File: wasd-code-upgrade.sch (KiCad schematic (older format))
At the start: 22 parts, among them J101 Conn_ARM_JTAG_SWD_10, J102 TC2030, Q101 ZXTN08400BFF, Q102 ZXTP25020CFFTA, U101 STM32L422CBTx, U102 MIC5205-3.3YM5

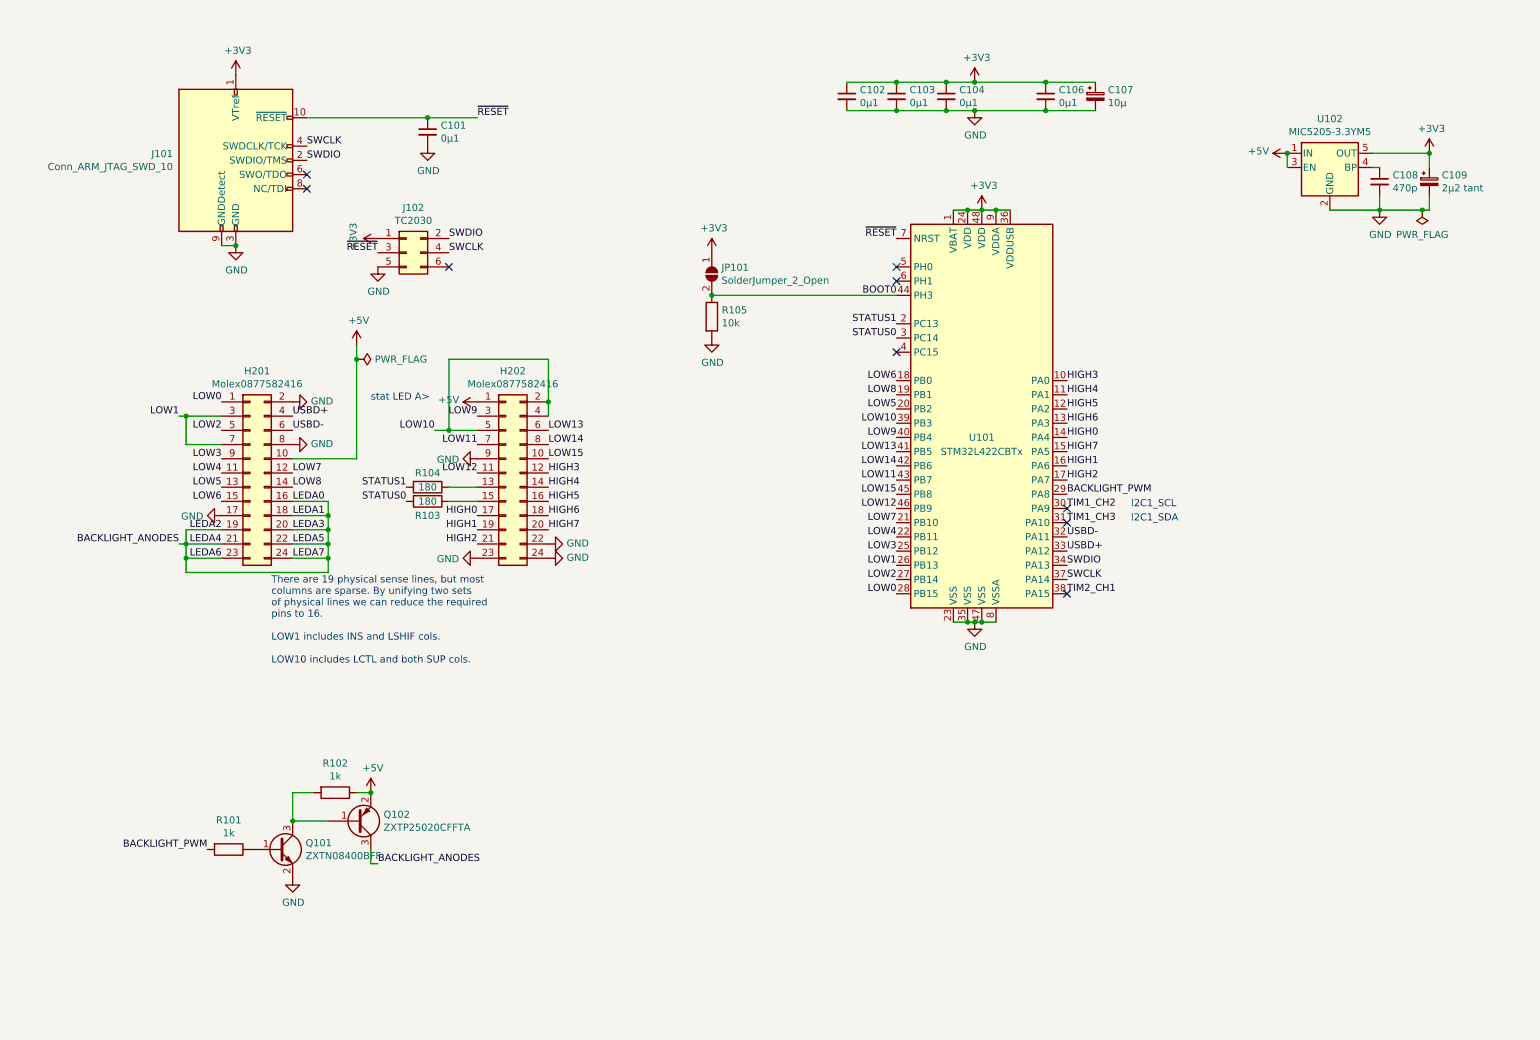
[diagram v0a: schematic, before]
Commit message: wasd-code-upgrade: schematic polish, matrix table
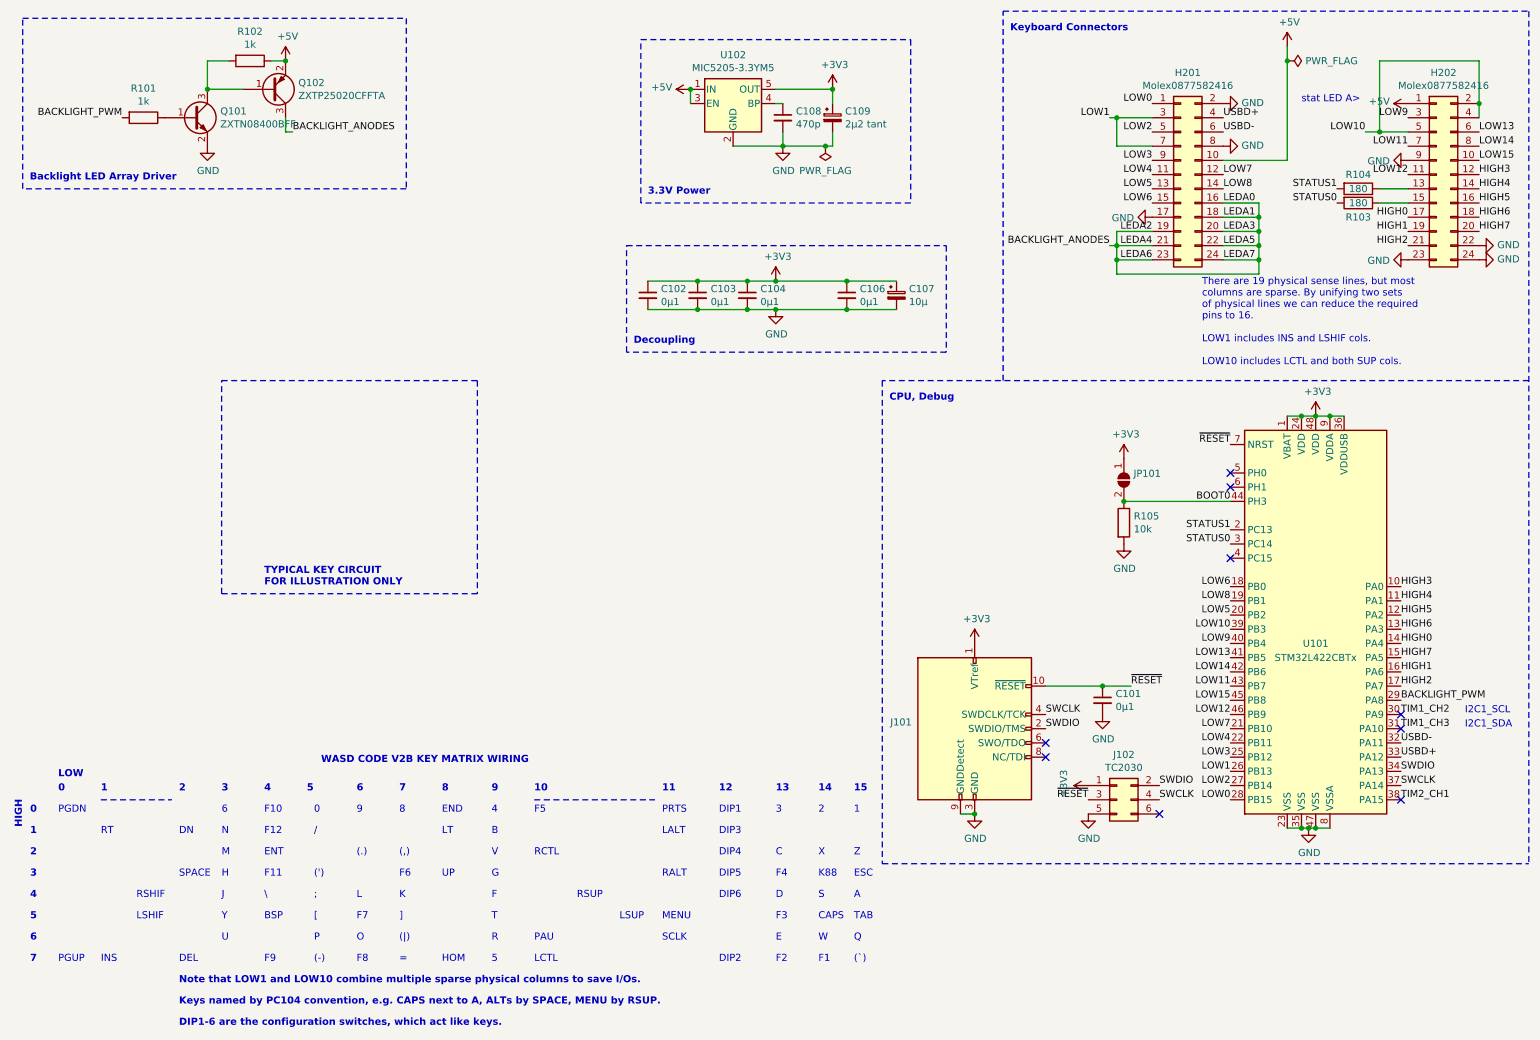
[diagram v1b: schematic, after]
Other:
- note added: "(')"
- note added: "(,)"
- note added: "(-)"
- note added: "(.)"
- note added: "(`)"
- note added: "(|)"
- note added: "/"
- note added: "0"
- note added: "1"
- note added: "10"
- note added: "11"
- note added: "12"
- note added: "13"
- note added: "14"
- note added: "15"
- note added: "2"
- note added: "3"
- note added: "3.3V Power"
- note added: "4"
- note added: "5"
- note added: "6"
- note added: "7"
- note added: "8"
- note added: "9"
- note added: ";"
- note added: "="
- note added: "A"
- note added: "B"
- note added: "BSP"
- note added: "Backlight LED Array Driver"
- note added: "C"
- note added: "CAPS"
- note added: "CPU, Debug"
- note added: "D"
- note added: "DEL"
- note added: "DIP1"
- note added: "DIP1-6 are the configuration switches, which act like keys."
- note added: "DIP2"
- note added: "DIP3"
- note added: "DIP4"
- note added: "DIP5"
- note added: "DIP6"
- note added: "DN"
- note added: "Decoupling"
- note added: "E"
- note added: "END"
- note added: "ENT"
- note added: "ESC"
- note added: "F"
- note added: "F1"
- note added: "F10"
- note added: "F11"
- note added: "F12"
- note added: "F2"
- note added: "F3"
- note added: "F4"
- note added: "F5"
- note added: "F6"
- note added: "F7"
- note added: "F8"
- note added: "F9"
- note added: "G"
- note added: "H"
- note added: "HIGH"
- note added: "HOM"
- note added: "INS"
- note added: "J"
- note added: "K"
- note added: "K88"
- note added: "Keyboard Connectors"
- note added: "Keys named by PC104 convention, e.g. CAPS next to A, ALTs by SPACE, MENU by RSUP."
- note added: "L"
- note added: "LALT"
- note added: "LCTL"
- note added: "LOW"
- note added: "LSHIF"
- note added: "LSUP"
- note added: "LT"
- note added: "M"
- note added: "MENU"
- note added: "N"
- note added: "Note that LOW1 and LOW10 combine multiple sparse physical columns to save I/Os."
- note added: "O"
- note added: "P"
- note added: "PAU"
- note added: "PGDN"
- note added: "PGUP"
- note added: "PRTS"
- note added: "Q"
- note added: "R"
- note added: "RALT"
- note added: "RCTL"
- note added: "RSHIF"
- note added: "RSUP"
- note added: "RT"
- note added: "S"
- note added: "SCLK"
- note added: "SPACE"
- note added: "T"
- note added: "TAB"
- note added: "TYPICAL KEY CIRCUIT\nFOR ILLUSTRATION ONLY"
- note added: "U"
- note added: "UP"
- note added: "V"
- note added: "W"
- note added: "WASD CODE V2B KEY MATRIX WIRING"
- note added: "X"
- note added: "Y"
- note added: "Z"
- note added: "["
- note added: "\"
- note added: "]"
- moved on the sheet: C101, C102, C103, C104, C106, C107, C108, C109, H201, H202, J101, J102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

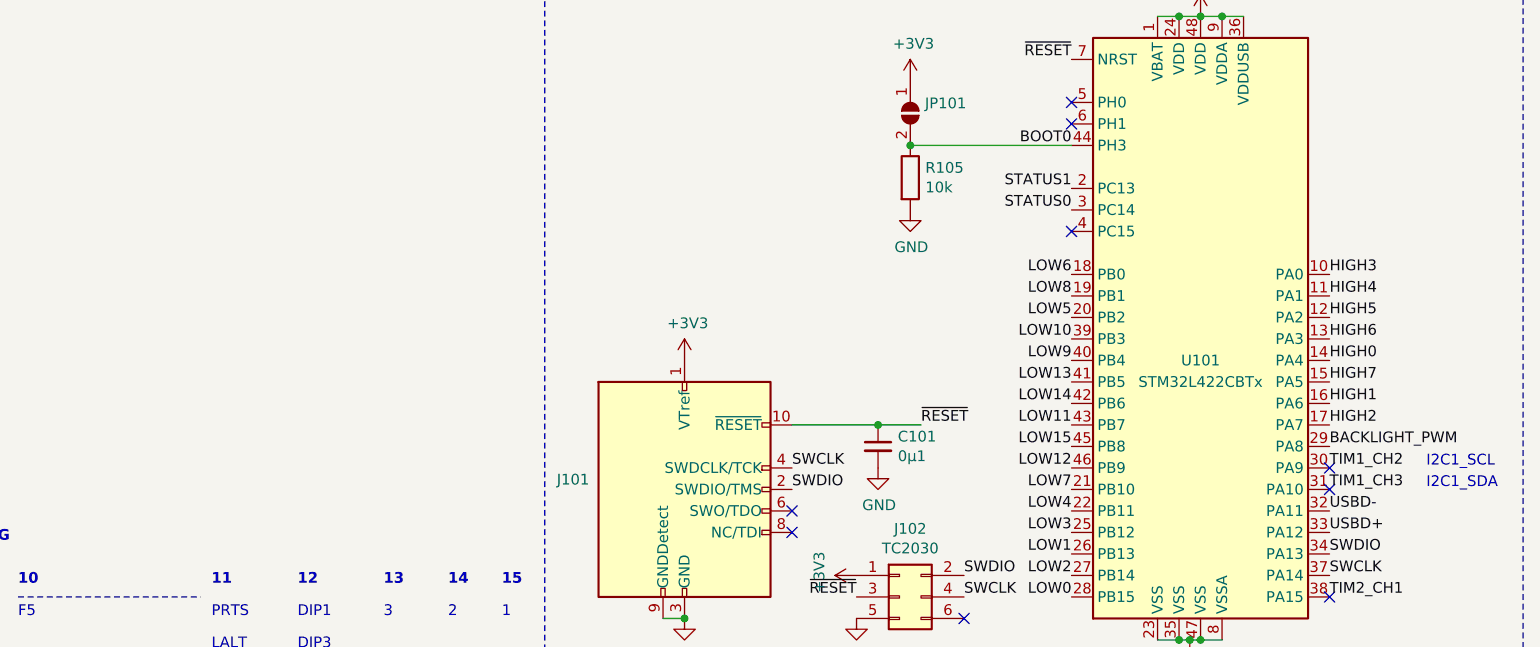
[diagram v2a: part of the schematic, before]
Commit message: wasd-code-upgrade: high side decoder simplifies routing
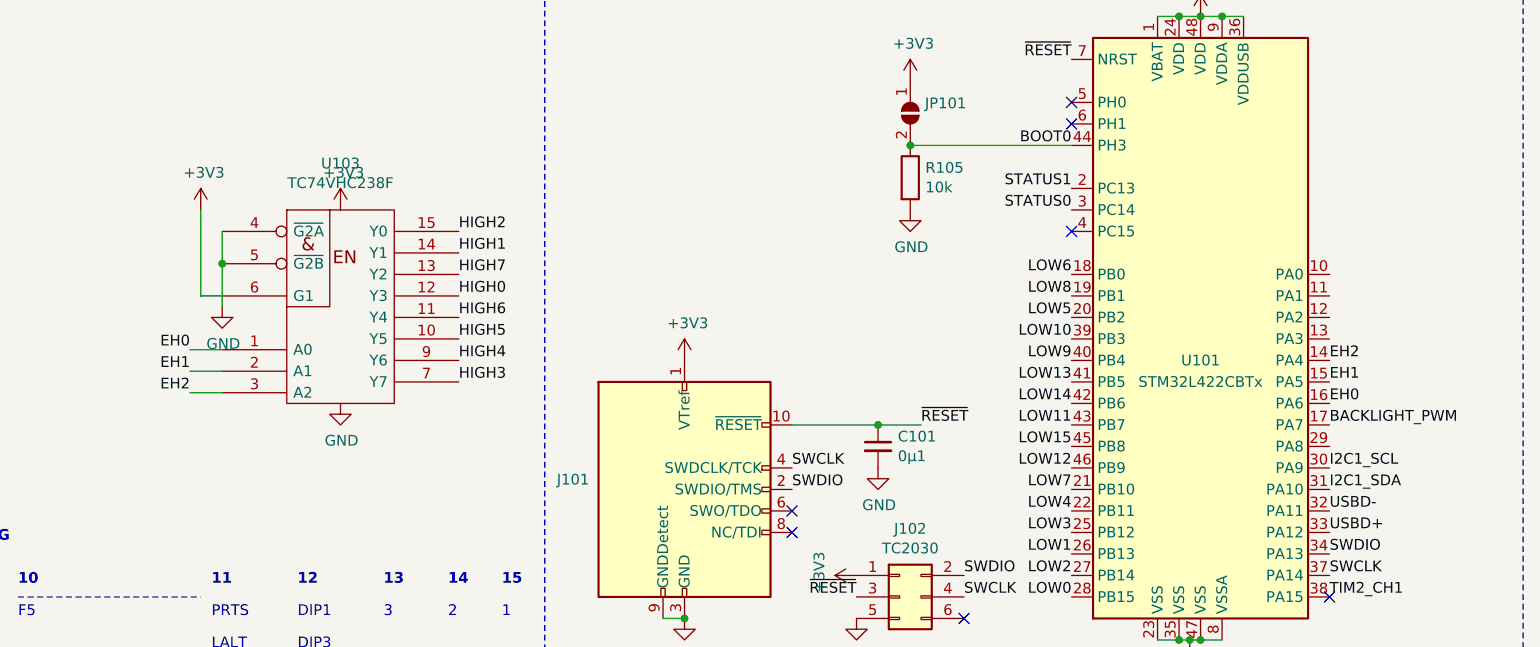
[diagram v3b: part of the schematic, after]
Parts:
- added U103: TC74VHC238F, vssop:VSSOP-16_3.0x4.25mm_P0.5mm, symbol 74xx_IEEE:74HC238
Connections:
- net +3V3: now also U103.16 (VCC), U103.6 (G1)
- net BACKLIGHT_PWM: now also U101.17 (PA7); no longer U101.29 (PA8)
- net GND: now also U103.4 (~G2A), U103.5 (~G2B), U103.8 (GND)
- net HIGH0: now also U103.12 (Y3); no longer U101.14 (PA4)
- net HIGH1: now also U103.14 (Y1); no longer U101.16 (PA6)
- net HIGH2: now also U103.15 (Y0); no longer U101.17 (PA7)
- net HIGH3: now also U103.7 (Y7); no longer U101.10 (PA0)
- net HIGH4: now also U103.9 (Y6); no longer U101.11 (PA1)
- net HIGH5: now also U103.10 (Y5); no longer U101.12 (PA2)
- net HIGH6: now also U103.11 (Y4); no longer U101.13 (PA3)
- net HIGH7: now also U103.13 (Y2); no longer U101.15 (PA5)
- net TIM1_CH2 renamed I2C1_SCL
- net TIM1_CH3 renamed I2C1_SDA
- new net EH0: U101.16 (PA6), U103.1 (A0)
- new net EH1: U101.15 (PA5), U103.2 (A1)
- new net EH2: U101.14 (PA4), U103.3 (A2)
- no-connect marks 9 -> 7
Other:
- note removed: "I2C1_SCL"
- note removed: "I2C1_SDA"
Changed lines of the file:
@@
 	1    0    0    -1
 $EndComp
-Text Label 10300 4950 0    50   ~ 0
-HIGH0
-Text Label 10300 5150 0    50   ~ 0
-HIGH1
-Text Label 10300 5250 0    50   ~ 0
-HIGH2
-Text Label 10300 4550 0    50   ~ 0
-HIGH3
-Text Label 10300 4650 0    50   ~ 0
-HIGH4
-Text Label 10300 4750 0    50   ~ 0
-HIGH5
-Text Label 10300 4850 0    50   ~ 0
-HIGH6
-Text Label 10300 5050 0    50   ~ 0
-HIGH7
 Text Label 9100 6050 2    50   ~ 0
 LOW0
@@
 NoConn ~ 9100 3750
 NoConn ~ 9100 3850
-NoConn ~ 10300 5450
-NoConn ~ 10300 5550
 NoConn ~ 10300 6050
 Text Label 9100 5050 2    50   ~ 0
@@
 ~RESET
 Text Label 10300 5450 0    50   ~ 0
-TIM1_CH2
+I2C1_SCL
 Text Label 10300 5550 0    50   ~ 0
-TIM1_CH3
+I2C1_SDA
 Text Label 10300 6050 0    50   ~ 0
 TIM2_CH1
@@
 Wire Wire Line
 	9300 2150 9300 2250
-Text Notes 10750 5450 0    50   ~ 0
-I2C1_SCL
-Text Notes 10750 5550 0    50   ~ 0
-I2C1_SDA
 $Comp
 L Device:C_Small C102
@@
 Text Label 9100 4250 2    50   ~ 0
 STATUS0
-Text Label 10300 5350 0    50   ~ 0
+Text Label 10300 5250 0    50   ~ 0
 BACKLIGHT_PWM
 NoConn ~ 9100 4350
@@
 Text Notes 1700 7650 0    50   ~ 10
 DIP1-6 are the configuration switches, which act like keys.
+$Comp
+L power:+3V3 #PWR0126
+U 1 1 5F3B29C9
+P 5700 4250
+F 0 "#PWR0126" H 5700 4100 50  0001 C CNN
+F 1 "+3V3" H 5715 4423 50  0000 C CNN
+F 2 "" H 5700 4250 50  0001 C CNN
+F 3 "" H 5700 4250 50  0001 C CNN
+	1    5700 4250
+	1    0    0    -1
+$EndComp
+$Comp
+L power:GND #PWR0127
+U 1 1 5F3B302B
+P 5700 5150
+F 0 "#PWR0127" H 5700 4900 50  0001 C CNN
+F 1 "GND" H 5705 4977 50  0000 C CNN
+F 2 "" H 5700 5150 50  0001 C CNN
+F 3 "" H 5700 5150 50  0001 C CNN
+	1    5700 5150
+	1    0    0    -1
+$EndComp
+Wire Wire Line
+	5150 4650 5050 4650
+Wire Wire Line
+	5050 4650 5050 4250
+$Comp
+L power:+3V3 #PWR0128
+U 1 1 5F3B62DA
+P 5050 4250
+F 0 "#PWR0128" H 5050 4100 50  0001 C CNN
+F 1 "+3V3" H 5065 4423 50  0000 C CNN
+F 2 "" H 5050 4250 50  0001 C CNN
+F 3 "" H 5050 4250 50  0001 C CNN
+	1    5050 4250
+	1    0    0    -1
+$EndComp
+$Comp
+L 74xx_IEEE:74HC238 U103
+U 1 1 5F3A148E
+P 5700 4550
+F 0 "U103" H 5700 5066 50  0000 C CNN
+F 1 "TC74VHC238F" H 5700 4975 50  0000 C CNN
+F 2 "vssop:VSSOP-16_3.0x4.25mm_P0.5mm" H 5700 4550 50  0001 C CNN
+F 3 "" H 5700 4550 50  0001 C CNN
+	1    5700 4550
+	1    0    0    -1
+$EndComp
+Wire Wire Line
+	5150 4350 5150 4500
+Connection ~ 5150 4500
+$Comp
+L power:GND #PWR0129
+U 1 1 5F3BB24A
+P 5150 4700
+F 0 "#PWR0129" H 5150 4450 50  0001 C CNN
+F 1 "GND" H 5155 4527 50  0000 C CNN
+F 2 "" H 5150 4700 50  0001 C CNN
+F 3 "" H 5150 4700 50  0001 C CNN
+	1    5150 4700
+	1    0    0    -1
+$EndComp
+Wire Wire Line
+	5150 4900 5000 4900
+Wire Wire Line
+	5150 5000 5000 5000
+Wire Wire Line
+	5150 5100 5000 5100
+Text Label 5000 4900 2    50   ~ 0
+EH0
+Text Label 5000 5000 2    50   ~ 0
+EH1
+Text Label 5000 5100 2    50   ~ 0
+EH2
+Text Label 6250 5050 0    50   ~ 0
+HIGH3
+Text Label 6250 4950 0    50   ~ 0
+HIGH4
+Text Label 6250 4850 0    50   ~ 0
+HIGH5
+Text Label 6250 4750 0    50   ~ 0
+HIGH6
+Text Label 6250 4650 0    50   ~ 0
+HIGH0
+Text Label 6250 4550 0    50   ~ 0
+HIGH7
+Text Label 6250 4450 0    50   ~ 0
+HIGH1
+Text Label 6250 4350 0    50   ~ 0
+HIGH2
+Wire Wire Line
+	5150 4500 5150 4700
+Text Label 10300 5150 0    50   ~ 0
+EH0
+Text Label 10300 5050 0    50   ~ 0
+EH1
+Text Label 10300 4950 0    50   ~ 0
+EH2
 $EndSCHEMATC

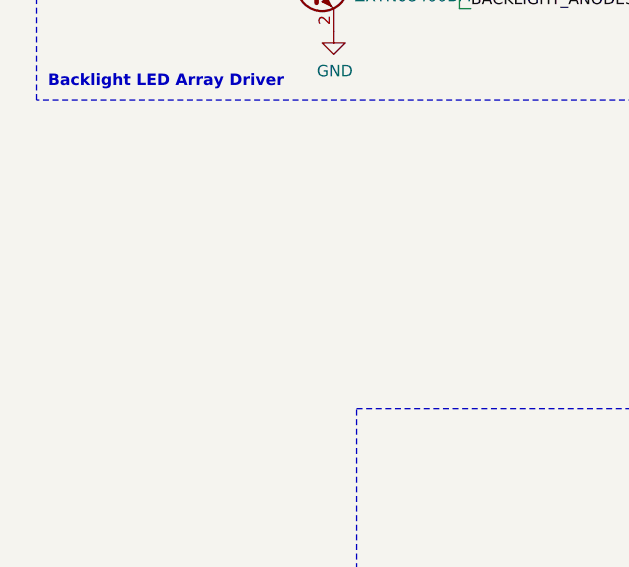
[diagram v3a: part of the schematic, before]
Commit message: wasd-code-upgrade: socket for MakerFocus OLED
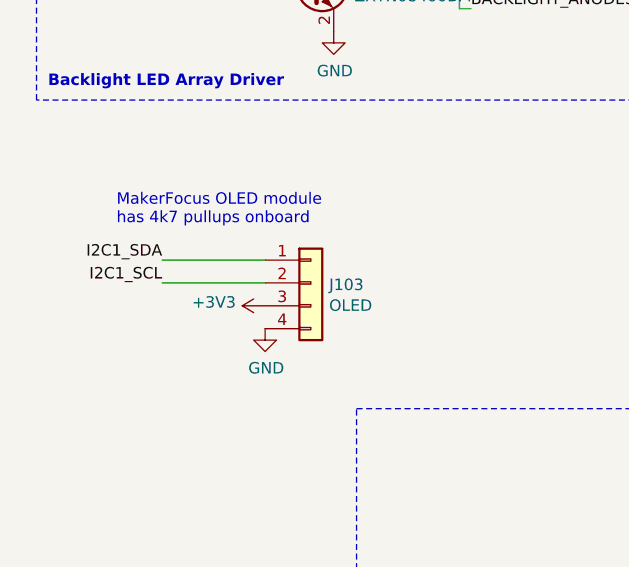
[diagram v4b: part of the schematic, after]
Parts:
- added J103: OLED, Connector_PinSocket_2.54mm:PinSocket_1x04_P2.54mm_Vertical_SMD_Pin1Left, symbol Connector_Generic:Conn_01x04
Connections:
- net +3V3: now also J103.3 (Pin_3)
- net GND: now also J103.4 (Pin_4)
- net I2C1_SCL: now also J103.2 (Pin_2)
- net I2C1_SDA: now also J103.1 (Pin_1)
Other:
- note added: "MakerFocus OLED module\nhas 4k7 pullups onboard"
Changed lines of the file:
@@
 Text Label 10300 4950 0    50   ~ 0
 EH2
+$Comp
+L Connector_Generic:Conn_01x04 J103
+U 1 1 5F3EFF40
+P 1800 2550
+F 0 "J103" H 1880 2542 50  0000 L CNN
+F 1 "OLED" H 1880 2451 50  0000 L CNN
+F 2 "Connector_PinSocket_2.54mm:PinSocket_1x04_P2.54mm_Vertical_SMD_Pin1Left" H 1800 2550 50  0001 C CNN
+F 3 "~" H 1800 2550 50  0001 C CNN
+	1    1800 2550
+	1    0    0    -1
+$EndComp
+$Comp
+L power:GND #PWR0130
+U 1 1 5F3F060A
+P 1600 2750
+F 0 "#PWR0130" H 1600 2500 50  0001 C CNN
+F 1 "GND" H 1605 2577 50  0000 C CNN
+F 2 "" H 1600 2750 50  0001 C CNN
+F 3 "" H 1600 2750 50  0001 C CNN
+	1    1600 2750
+	1    0    0    -1
+$EndComp
+$Comp
+L power:+3V3 #PWR0131
+U 1 1 5F3F136D
+P 1600 2650
+F 0 "#PWR0131" H 1600 2500 50  0001 C CNN
+F 1 "+3V3" V 1615 2778 50  0000 L CNN
+F 2 "" H 1600 2650 50  0001 C CNN
+F 3 "" H 1600 2650 50  0001 C CNN
+	1    1600 2650
+	0    -1   -1   0
+$EndComp
+Wire Wire Line
+	1600 2450 1150 2450
+Text Label 1150 2450 2    50   ~ 0
+I2C1_SDA
+Text Label 1150 2550 2    50   ~ 0
+I2C1_SCL
+Wire Wire Line
+	1150 2550 1600 2550
+Text Notes 950  2300 0    50   ~ 0
+MakerFocus OLED module\nhas 4k7 pullups onboard
 $EndSCHEMATC
